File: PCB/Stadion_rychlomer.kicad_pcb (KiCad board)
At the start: 4 copper layers, 44 x 44 mm, 38 parts, among them J2 OLED I2C, J3 ICSP, J4 Conn_01x03_Pin, J5 SPÍD & PWR, J6 AUX DDAA, J7 ENG RPM, Q1 140817143200, U1 Mikroprofesor, U3 LM1117MP-5.0, Y1 16MHz

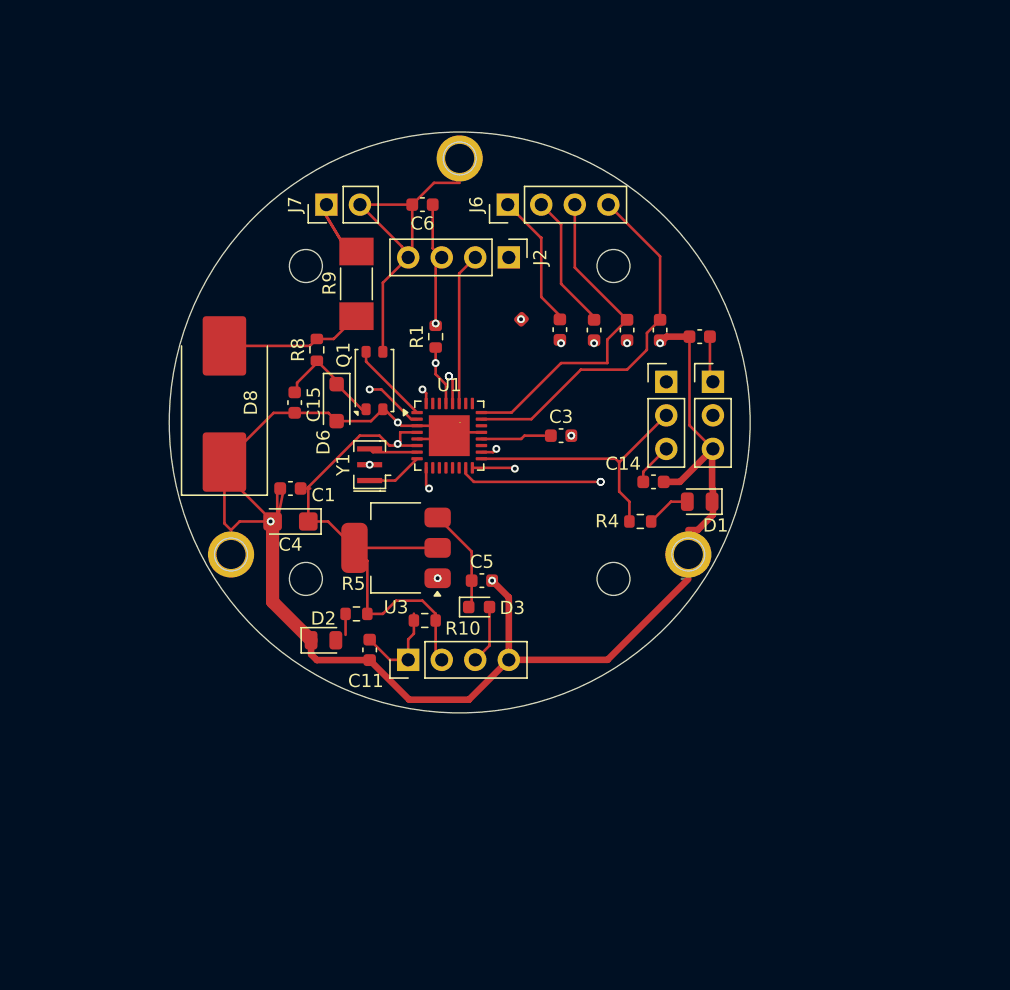
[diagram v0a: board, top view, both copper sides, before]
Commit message: SPD Optocoupler ESD Protection
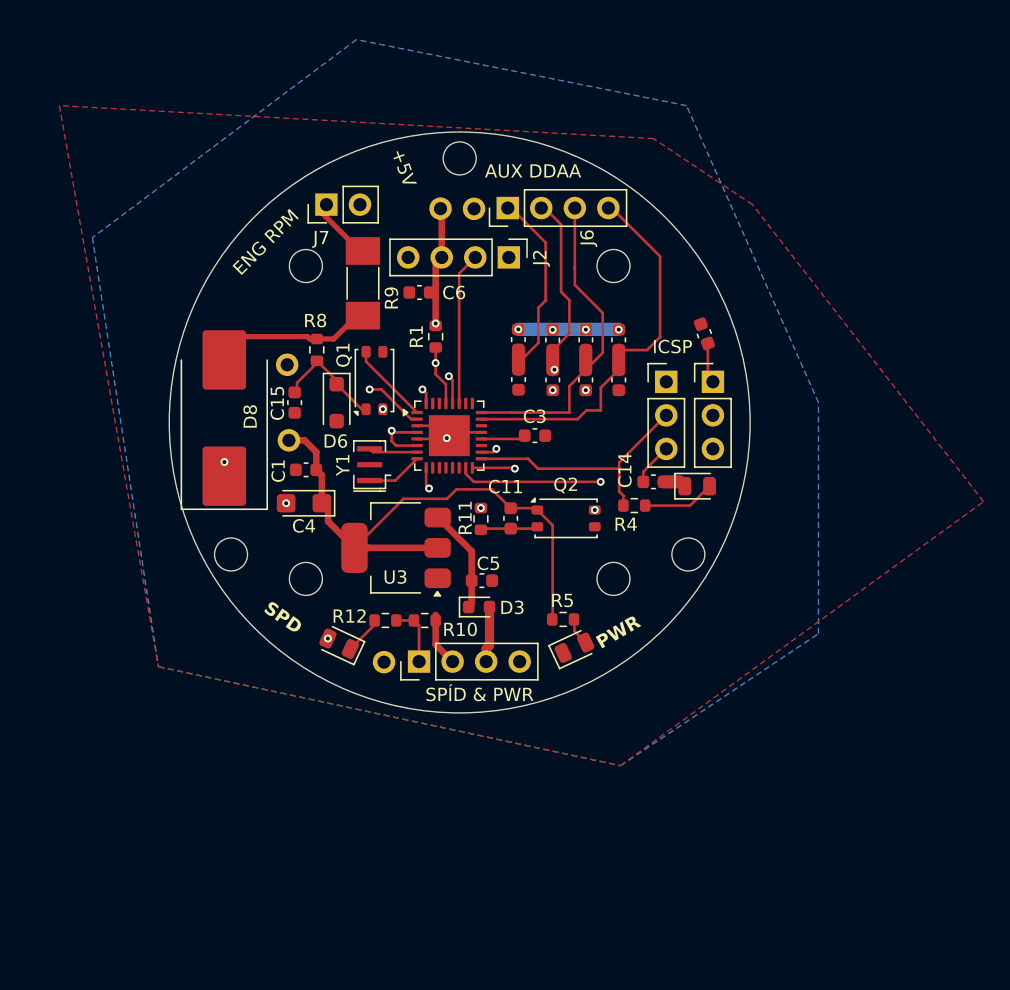
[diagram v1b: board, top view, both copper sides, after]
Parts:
- removed the ? at (122.5, 136.2)
- removed H1, H2, H3: 2mm, MountingHole:MountingHole_2.2mm_M2_ISO7380_Pad
- added ?: , , F.Cu at (112.1, 162.2)
- added ?: , , F.Cu at (116.4, 127.8)
- added ?: , Capacitor_SMD:C_0603_1608Metric, F.Cu at (127.4, 137.7)
- added ?: , , F.Cu at (118.9, 127.8)
- added ?: , Capacitor_SMD:C_0603_1608Metric, F.Cu at (122.3, 137.7)
- added ?: , , F.Cu at (104.9, 145.4)
- added ?: , Capacitor_SMD:C_0603_1608Metric, F.Cu at (124.9, 137.8)
- added ?: , , F.Cu at (104.8, 139.6)
- added ?: , Capacitor_SMD:C_0603_1608Metric, F.Cu at (129.9, 137.7)
- added D7: Yellow, LED_SMD:LED_0805_2012Metric, F.Cu at (108.7, 160.8)
- added Q2: PC817, OptoDevice:Panasonic_APV-AQY_SSOP-4_4.45x2.65mm_P1.27mm, F.Cu at (125.9, 151.3)
- added R11: 470R, Resistor_SMD:R_0603_1608Metric, F.Cu at (119.4, 151.3)
- added R12: 1k, Resistor_SMD:R_0603_1608Metric, F.Cu at (112.2, 159.0)
- ? (x2): renamed from C12; value 100n -> (none)
- R10: value 15k -> 10k
- moved D2 19.0 mm to (126.5, 161.1), turned to 25 degrees
- moved R5 15.7 mm to (125.7, 158.9), turned to 0 degrees
- moved C11 14.6 mm to (121.7, 151.3)
- moved C6 6.66 mm to (114.8, 134.2)
- moved ? 4.91 mm to (122.3, 140.8)
- moved ? 4.91 mm to (124.9, 140.8)
- moved C12 4.91 mm to (127.4, 140.8)
- moved C13 4.91 mm to (129.9, 140.8)
- moved C3 1.98 mm to (123.5, 145.0)
- moved C1 1.84 mm to (106.2, 147.6)
- moved C4 1.72 mm to (106.0, 150.1)
- moved R4 1.29 mm to (131.0, 150.3)
- moved D1 1.19 mm to (135.8, 148.8), turned to 0 degrees
- moved D8 1.07 mm to (100.0, 143.7)
- moved J5 0.83 mm to (114.7, 162.1)
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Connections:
- ? pad 1: (no net) -> /D4_AUX
- ? pad 2: (no net) -> GND (x2)
- ? pad 1: (no net) -> /D5_AUX
- C11 pad 1: /D2_SPD -> +5V
- C11 pad 2: GND -> Net-(C11-Pad2)
- R10 pad 1: +5V -> /D2_SPD
- R10 pad 2: /D2_SPD -> +5V
- R9 pad 1: Net-(D8-A2) -> /D3_ENG_RPM
- R9 pad 2: /D3_ENG_RPM -> Net-(D8-A2)
- U1 pad 32: /D2_SPD -> Net-(U1-PD2)
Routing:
- net GND: track 227.8 -> 12.1 mm, vias 11 -> 6
- net +5V: track 109.7 -> 139.3 mm, vias 4 -> 8
- net Net-(U1-PD2): track 0.00 -> 18.4 mm, vias 0 -> 2
- net /D2_SPD: track 29.9 -> 19.1 mm
- net /D5_AUX: track 38.9 -> 30.6 mm, vias 1 -> 2
- net /D4_AUX: track 37.9 -> 43.2 mm
- net Net-(C11-Pad2): track 0.00 -> 4.37 mm
- net /D11/MOSI_: track 26.4 -> 22.8 mm, vias 2 -> 1
- net Net-(D7-K): track 0.00 -> 2.59 mm
- net Net-(D1-A): track 3.36 -> 5.51 mm
- net /A0_AUX: track 27.7 -> 29.7 mm
- net Net-(U1-AREF): track 4.86 -> 3.36 mm
- net /D13/SCK_: track 20.4 -> 19.3 mm
- net /I2C_SDA: vias 3 -> 1
- added copper zone on B.Cu, net GND
- added copper zone on F.Cu, net GND
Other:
- outline, holes or cut-outs redrawn
- board text added: "+5V"
- board text added: "+5V MISO"
- board text added: "A0 A1 D5 D4"
- board text added: "AUX"
- board text added: "GND"
- board text added: "GND 5V"
- board text added: "GND RES"
- board text added: "GND VCC 5V SPD GND"
- board text added: "ICSP"
- board text added: "MOPeD JESUS STADI-SPÍDo V1"
- board text added: "MOSI SCK"
- board text added: "PWR"
- board text added: "RPM"
- board text added: "SDA SCL 5V GND"
- board text added: "SPD"
- board text added: "SPÍD"
- board text added: "STS CHVOJKOVICE-BROD + KATODA OLOMÓC"

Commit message: Ferrite beads add
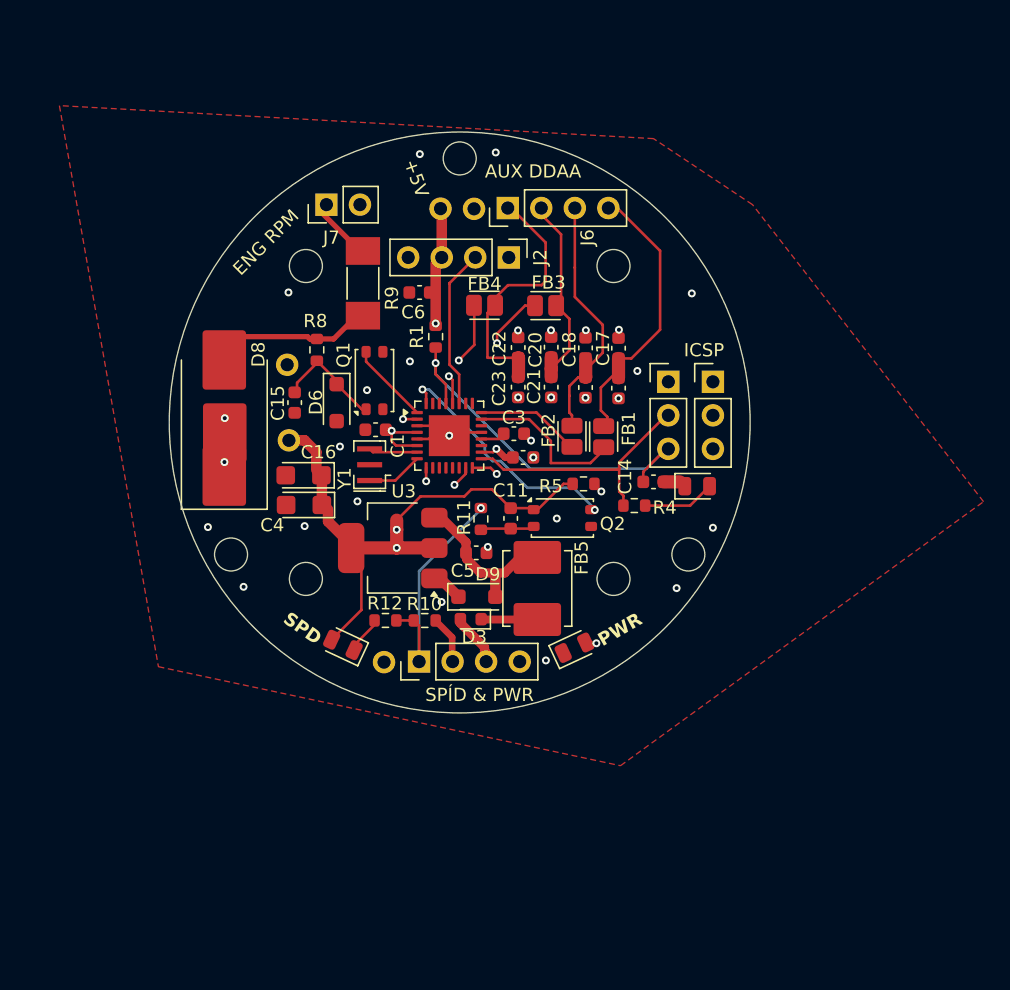
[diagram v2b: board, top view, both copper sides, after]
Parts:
- removed the ? at (122.3, 140.8)
- removed the ? at (127.4, 137.7)
- removed the ? at (122.3, 137.7)
- removed the ? at (124.9, 137.8)
- removed the ? at (124.9, 140.8)
- removed the ? at (129.9, 137.7)
- added ?: , , F.Cu at (100.0, 144.8)
- added C16: 4u7_16V, Capacitor_Tantalum_SMD:CP_EIA-3216-10_Kemet-I, F.Cu at (106.0, 148.0)
- added C17: 100n, Capacitor_SMD:C_0603_1608Metric, F.Cu at (129.8, 138.4)
- added C18: 100n, Capacitor_SMD:C_0603_1608Metric, F.Cu at (127.3, 138.3)
- added C20: 100n, Capacitor_SMD:C_0603_1608Metric, F.Cu at (124.8, 138.3)
- added C21: 100n, Capacitor_SMD:C_0603_1608Metric, F.Cu at (124.8, 141.3)
- added C22: 100n, Capacitor_SMD:C_0603_1608Metric, F.Cu at (122.2, 138.3)
- added C23: 100n, Capacitor_SMD:C_0603_1608Metric, F.Cu at (122.2, 141.3)
- added D9: SMCJ85CA, Diode_SMD:D_SOD-123F, F.Cu at (119.1, 157.2)
- added FB1: FerriteBead_Small, Inductor_SMD:L_Eaton_MCL2012V1, F.Cu at (128.7, 145.1)
- added FB2: FerriteBead_Small, Inductor_SMD:L_Eaton_MCL2012V1, F.Cu at (126.3, 145.1)
- added FB3: FerriteBead_Small, Inductor_SMD:L_Eaton_MCL2012V1, F.Cu at (124.3, 135.2)
- added FB4: FerriteBead_Small, Inductor_SMD:L_Eaton_MCL2012V1, F.Cu at (119.7, 135.1)
- added FB5: FerriteBead_Small, Inductor_SMD:L_Panasonic_PCC-M0530M, F.Cu at (123.7, 156.6)
- moved C2 16.6 mm to (122.6, 146.7), turned to 0 degrees
- moved R5 10.4 mm to (127.2, 148.7)
- moved C1 6.08 mm to (111.5, 144.6)
- moved C5 2.15 mm to (119.1, 153.9)
- moved C3 1.60 mm to (121.9, 144.8)
- moved D3 1.12 mm to (118.7, 158.9), turned to 180 degrees
- moved C13 0.62 mm to (129.8, 141.4)
- moved C12 0.57 mm to (127.3, 141.3)
- moved D7 0.30 mm to (109.0, 160.8)
- moved Q2 0.28 mm to (125.6, 151.2)
- moved U3 0.25 mm to (112.8, 153.5)
- moved J4 0.16 mm to (133.6, 140.9)
- moved C4 0.13 mm to (106.0, 150.2)
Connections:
- ? pad 0: (no net) -> GND (x2)
- C5 pad 1: VCC -> Net-(D9-A2)
- U1 pad 2: /D4_AUX -> /D4
- U1 pad 23: /A0_AUX -> /A0
- U1 pad 24: /A1_AUX -> /A1
- U1 pad 9: /D5_AUX -> /D5
- U3 pad 3: VCC -> Net-(D9-A2)
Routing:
- net /D4_AUX: track 43.2 -> 20.3 mm, vias 1 -> 0
- net /D5: track 0.00 -> 21.5 mm, vias 0 -> 2
- net +5V: track 139.3 -> 123.8 mm, vias 8 -> 9
- net /D5_AUX: track 30.6 -> 15.7 mm, vias 2 -> 0
- net /D4: track 0.00 -> 14.9 mm, vias 0 -> 2
- net Net-(D2-A): track 1.65 -> 15.5 mm, vias 0 -> 2
- net /A0: track 0.00 -> 12.4 mm
- net Net-(D9-A2): track 0.00 -> 12.0 mm
- net /A1: track 0.00 -> 7.93 mm
- net /A0_AUX: track 29.7 -> 21.8 mm
- net /A1_AUX: track 25.8 -> 20.5 mm
- net VCC: track 7.95 -> 4.00 mm
- net /I2C_SDA: track 13.1 -> 16.7 mm
- net GND: track 12.1 -> 14.8 mm, vias 6 -> 27
- net /D11/MOSI_: track 22.8 -> 24.7 mm
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- added copper zone on In1.Cu, net GND
- removed copper zone on B.Cu, net GND
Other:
- board text added: "GND VIN 5V SPD GND"
- board text added: "MOPeD JeSUS STADi-SPÍDo V1"
- board text added: "STS CHVOJKOVICE-BROD / KATODA OLOMÓC"
- board text removed: "GND VCC 5V SPD GND"
- board text removed: "MOPeD JESUS STADI-SPÍDo V1"
- board text removed: "STS CHVOJKOVICE-BROD + KATODA OLOMÓC"

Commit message: Ordered in JLCPCB
Added GND Ferrite bead
Ordered in JLCPCB - stadisped.zip
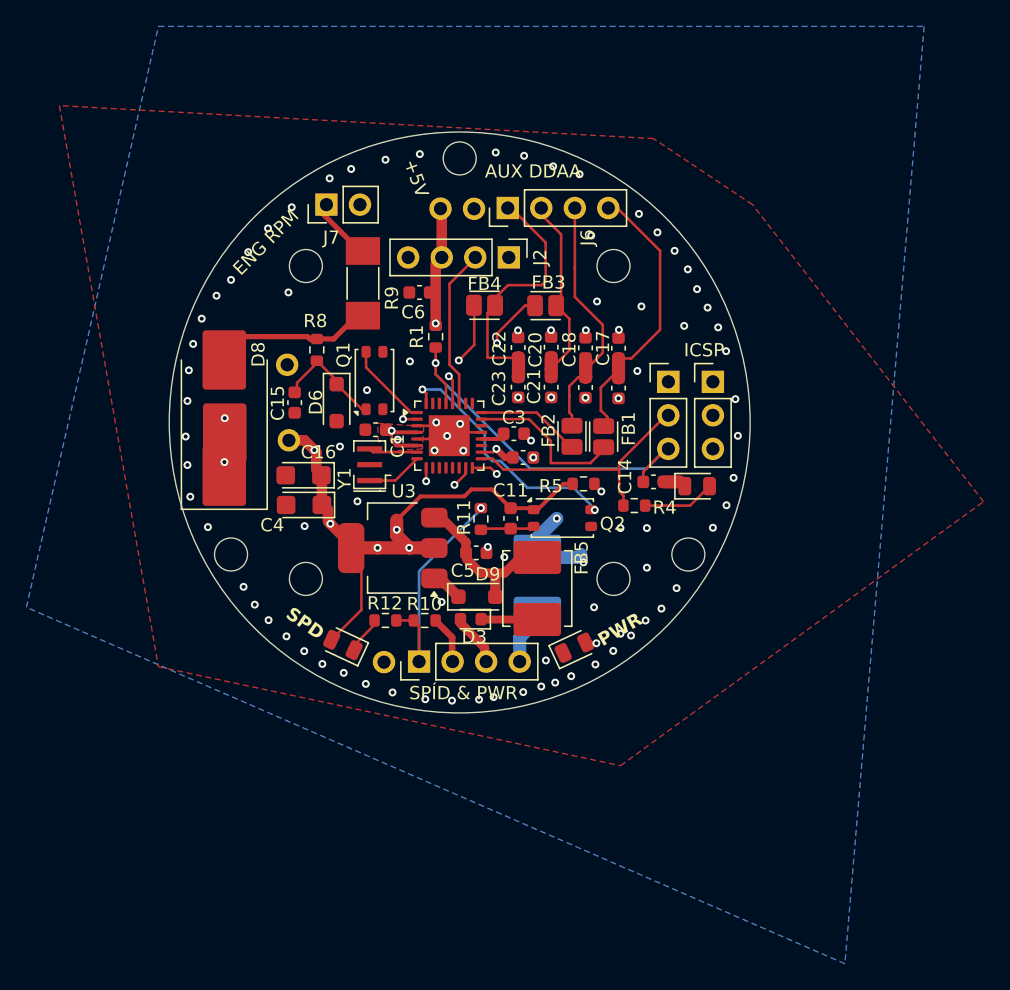
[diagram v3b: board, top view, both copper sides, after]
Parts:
- added FB6: FerriteBead_Small, Inductor_SMD:L_Panasonic_PCC-M0530M, B.Cu at (123.7, 156.1)
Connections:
- J5 pad 4: GND -> Net-(J5-Pin_4)
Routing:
- net GND: track 14.8 -> 21.4 mm, vias 27 -> 92
- net +5V: track 123.8 -> 118.4 mm, vias 9 -> 13
- net Net-(J5-Pin_4): track 0.00 -> 4.25 mm
- net Net-(U1-PD2): track 18.4 -> 18.9 mm
- added copper zone on F.Cu, net +5V
- added copper zone on In2.Cu, net +5V
- added copper zone on B.Cu, net GND

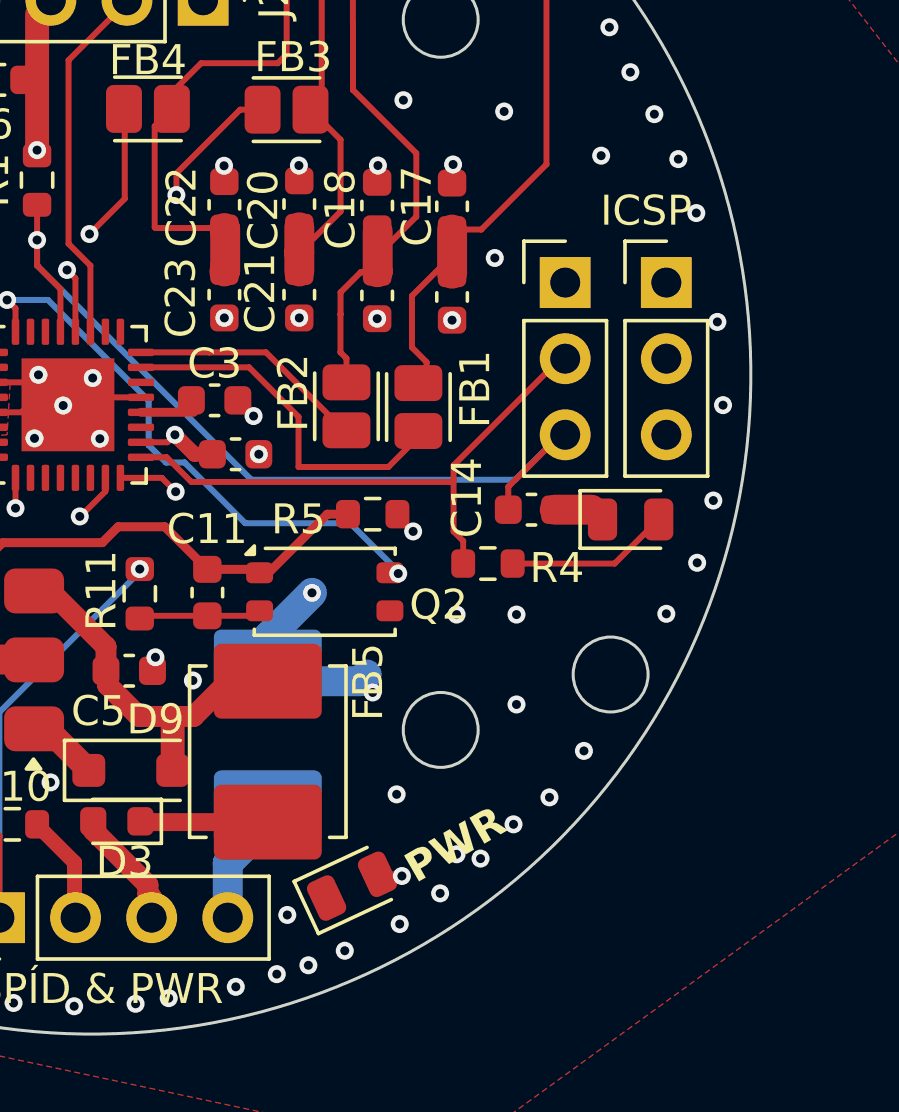
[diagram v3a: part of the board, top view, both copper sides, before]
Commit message: Update Silkprint a drobná škatulata
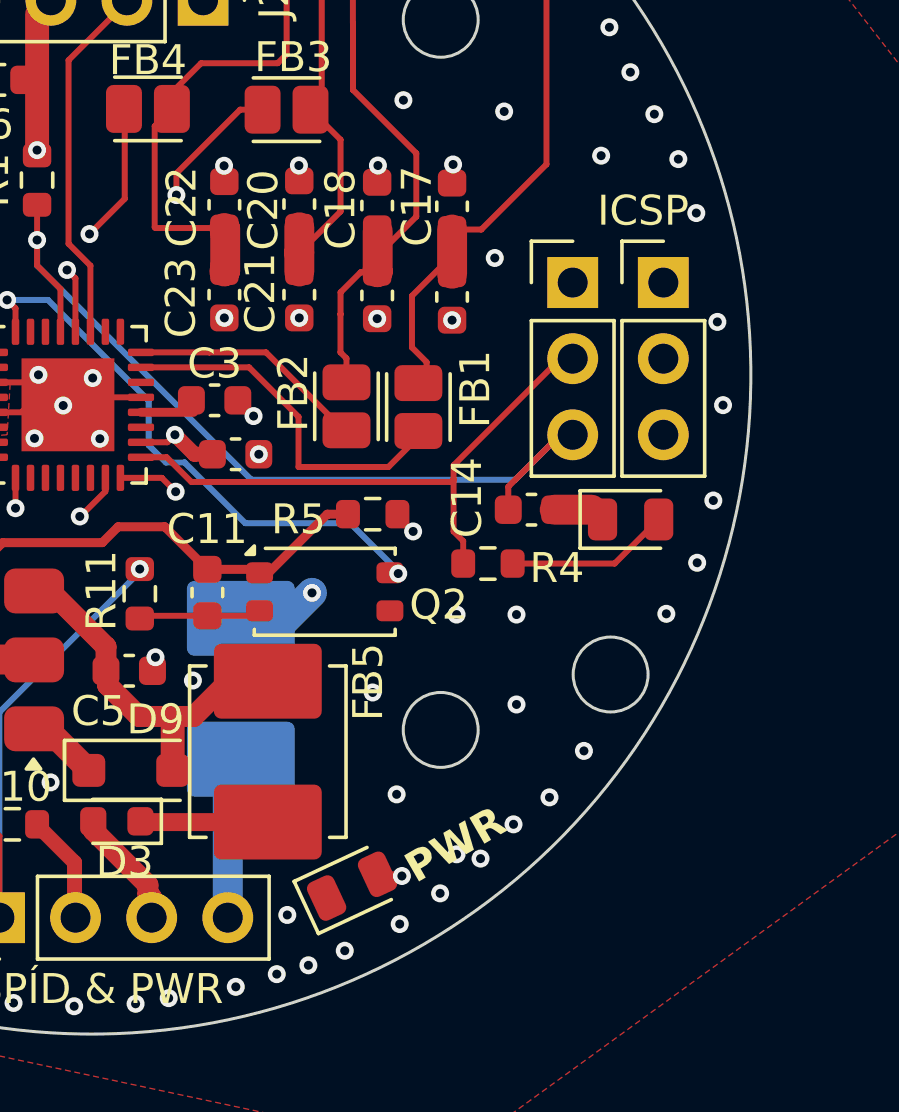
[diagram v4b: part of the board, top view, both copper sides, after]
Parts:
- moved FB6 1.86 mm to (122.8, 154.5)
- moved J4 0.25 mm to (133.9, 140.9)
- moved J3 0.10 mm to (136.9, 140.9)
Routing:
- net GND: track 21.4 -> 16.7 mm
- net Net-(J5-Pin_4): track 4.25 -> 6.20 mm
